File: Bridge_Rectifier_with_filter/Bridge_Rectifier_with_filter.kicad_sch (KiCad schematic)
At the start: 13 parts, among them J1 Screw_Terminal_01x02, J2 Conn_01x02_Pin, T1 Transformer_1P_1S

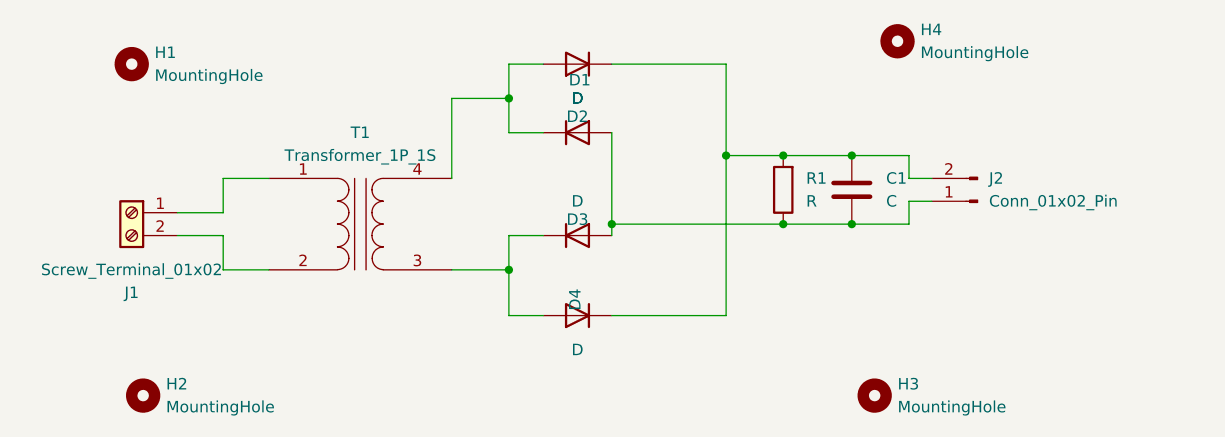
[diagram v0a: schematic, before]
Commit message: xenor regulator added in the bridge rectifier
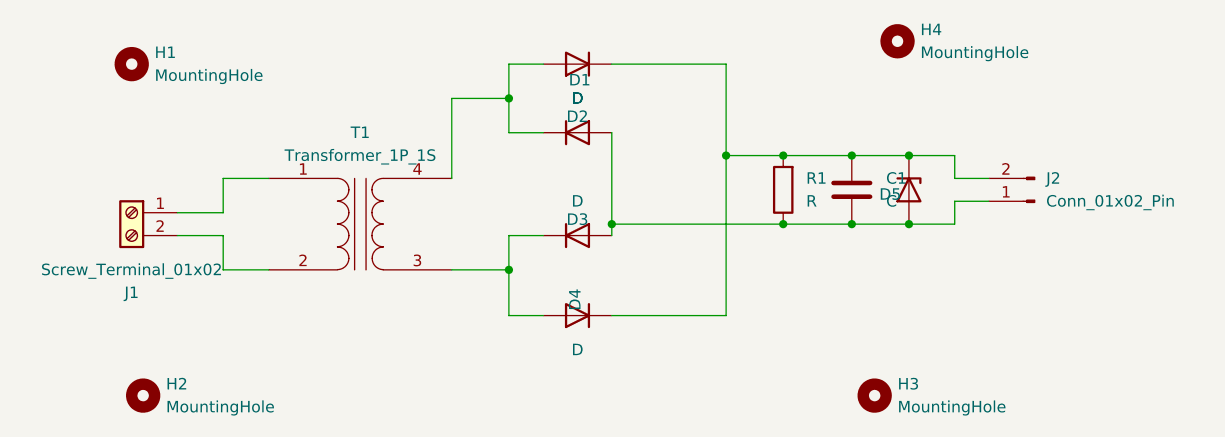
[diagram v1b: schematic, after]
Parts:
- added D5: D_Zener, Diode_SMD:D_SOD-323, symbol Device:D_Zener
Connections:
- net at C1.1, D1.1 (K), D4.1 (K)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: now also D5.1 (K)
- net at C1.2, D2.2 (A), D3.2 (A)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: now also D5.2 (A)
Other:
- moved on the sheet: J2
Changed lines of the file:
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@@
+	)
+	(junction
+		(at 148.59 76.2)
+		(diameter 0)
+		(color 0 0 0 0)
 	)
 	(junction
@@
 	)
 	(junction
+		(at 148.59 68.58)
+		(diameter 0)
+		(color 0 0 0 0)
+	)
+	(junction
 		(at 134.62 76.2)
 		(diameter 0)
@@
 	(wire
 		(pts
+			(xy 153.67 68.58) (xy 153.67 71.12)
+		)
+		(stroke
+			(width 0)
+			(type default)
+		)
+	)
+	(wire
+		(pts
 			(xy 115.57 76.2) (xy 115.57 77.47)
 		)
@@
 	(wire
 		(pts
-			(xy 148.59 73.66) (xy 148.59 76.2)
-		)
-		(stroke
-			(width 0)
-			(type default)
-		)
-	)
-	(wire
-		(pts
 			(xy 72.39 77.47) (xy 72.39 81.28)
 		)
@@
 	(wire
 		(pts
-			(xy 148.59 73.66) (xy 151.13 73.66)
+			(xy 153.67 71.12) (xy 157.48 71.12)
 		)
 		(stroke
@@
 	(wire
 		(pts
-			(xy 148.59 71.12) (xy 151.13 71.12)
-		)
-		(stroke
-			(width 0)
-			(type default)
-		)
-	)
-	(wire
-		(pts
 			(xy 128.27 68.58) (xy 128.27 86.36)
 		)
@@
 	(wire
 		(pts
+			(xy 153.67 73.66) (xy 153.67 76.2)
+		)
+		(stroke
+			(width 0)
+			(type default)
+		)
+	)
+	(wire
+		(pts
 			(xy 134.62 76.2) (xy 142.24 76.2)
 		)
@@
 	(wire
 		(pts
-			(xy 148.59 68.58) (xy 148.59 71.12)
-		)
-		(stroke
-			(width 0)
-			(type default)
-		)
-	)
-	(wire
-		(pts
 			(xy 104.14 62.23) (xy 104.14 66.04)
 		)
@@
 	(wire
 		(pts
+			(xy 148.59 68.58) (xy 153.67 68.58)
+		)
+		(stroke
+			(width 0)
+			(type default)
+		)
+	)
+	(wire
+		(pts
 			(xy 104.14 81.28) (xy 104.14 86.36)
+		)
+		(stroke
+			(width 0)
+			(type default)
+		)
+	)
+	(wire
+		(pts
+			(xy 148.59 76.2) (xy 153.67 76.2)
+		)
+		(stroke
+			(width 0)
+			(type default)
+		)
+	)
+	(wire
+		(pts
+			(xy 153.67 73.66) (xy 157.48 73.66)
 		)
 		(stroke
@@
 	(symbol
 		(lib_id "Connector:Conn_01x02_Pin")
-		(at 156.21 73.66 180)
+		(at 162.56 73.66 180)
 		(unit 1)
 		(body_style 1)
@@
 		(dnp no)
 		(property "Reference" "J2"
-			(at 157.48 71.1199 0)
+			(at 163.83 71.1199 0)
 			(show_name no)
 			(do_not_autoplace no)
@@
 		)
 		(property "Value" "Conn_01x02_Pin"
-			(at 157.48 73.6599 0)
+			(at 163.83 73.6599 0)
 			(show_name no)
 			(do_not_autoplace no)
@@
 		)
 		(property "Footprint" "Connector_PinHeader_2.54mm:PinHeader_1x02_P2.54mm_Vertical_SMD_Pin1Right"
-			(at 156.21 73.66 0)
+			(at 162.56 73.66 0)
 			(hide yes)
 			(show_name no)
@@
 		)
 		(property "Datasheet" ""
-			(at 156.21 73.66 0)
+			(at 162.56 73.66 0)
 			(hide yes)
 			(show_name no)
@@
 		)
 		(property "Description" "Generic connector, single row, 01x02, script generated"
-			(at 156.21 73.66 0)
+			(at 162.56 73.66 0)
 			(hide yes)
 			(show_name no)
@@
 					(unit 1)
 				)
+			)
+		)
+	)
+	(symbol
+		(lib_id "Device:D_Zener")
+		(at 148.59 72.39 270)
+		(unit 1)
+		(body_style 1)
+		(exclude_from_sim no)
+		(in_bom yes)
+		(on_board yes)
+		(in_pos_files yes)
+		(dnp no)
+		(property "Reference" "D5"
+			(at 145.288 72.898 90)
+			(show_name no)
+			(do_not_autoplace no)
+			(effects
+				(font
+					(size 1.27 1.27)
+				)
+				(justify left)
+			)
+		)
+		(property "Value" "D_Zener"
+			(at 151.13 73.6599 90)
+			(hide yes)
+			(show_name no)
+			(do_not_autoplace no)
+			(effects
+				(font
+					(size 1.27 1.27)
+				)
+				(justify left)
+			)
+		)
+		(property "Footprint" "Diode_SMD:D_SOD-323"
+			(at 148.59 72.39 0)
+			(hide yes)
+			(show_name no)
+			(do_not_autoplace no)
+			(effects
+				(font
+					(size 1.27 1.27)
+				)
+			)
+		)
+		(property "Datasheet" ""
+			(at 148.59 72.39 0)
+			(hide yes)
+			(show_name no)
+			(do_not_autoplace no)
+			(effects
+				(font
+					(size 1.27 1.27)
+				)
+			)
+		)
+		(property "Description" "Zener diode"
+			(at 148.59 72.39 0)
+			(hide yes)
+			(show_name no)
+			(do_not_autoplace no)
+			(effects
+				(font
+					(size 1.27 1.27)
+				)
+			)
+		)
+		(pin "2"
+		)
+		(pin "1"
+		)
+		(instances
+			(project "Bridge_Rectifier_with_filter"
+				(path "/51f75efd-7f51-4969-bd5f-41b987d4fc89"
+					(reference "D5")
+					(unit 1)
+				)

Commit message: new clipper and clamper circuits are added
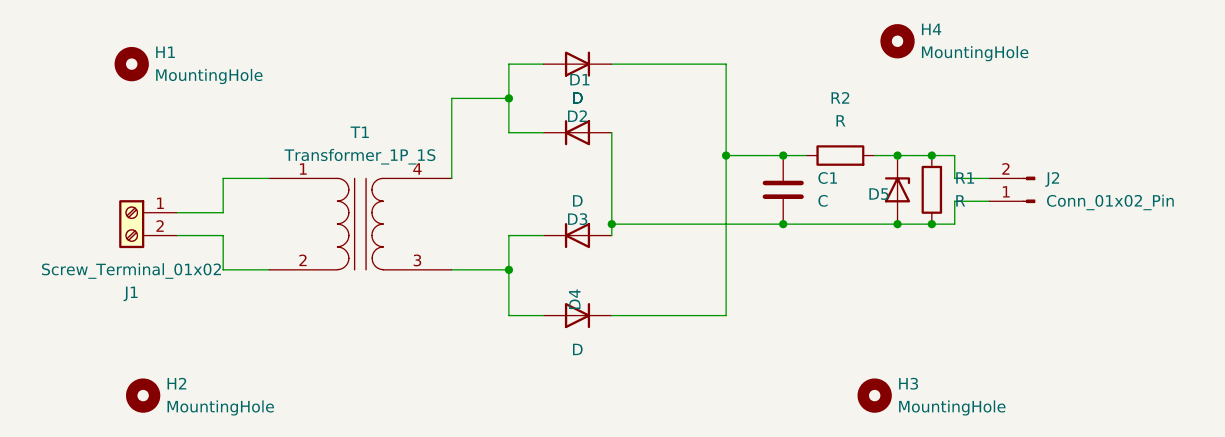
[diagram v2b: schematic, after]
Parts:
- added R2: R, Resistor_SMD:R_0603_1608Metric_Pad0.98x0.95mm_HandSolder, symbol Device:R
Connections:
- net at C1.1, D1.1 (K), D4.1 (K): now also R2.1; no longer D5.1 (K), J2.2 (Pin_2), R1.2
- new net: D5.1 (K), J2.2 (Pin_2), R1.2, R2.2
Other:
- moved on the sheet: C1, D5, R1
